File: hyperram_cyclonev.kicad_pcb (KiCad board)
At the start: 4 copper layers, 70.1 x 89.7 mm, 65 parts, among them IC1 AP63205WU, IC2 TXB0108PWR, IC3 S26KL128SDABHI020, IC4 W25Q32JVSSIQ_TR, IC5 S27KL0641DABHI020, J1 ASP-122952-01, J2 HDMI_A, J3 Conn_02x10_Odd_Even, J4 Conn_02x06_Odd_Even, J5 Conn_02x06_Top_Bottom, J6 Conn_02x06_Top_Bottom, J7 Conn_02x06_Top_Bottom, Q1 BSS138, Q2 BSS138

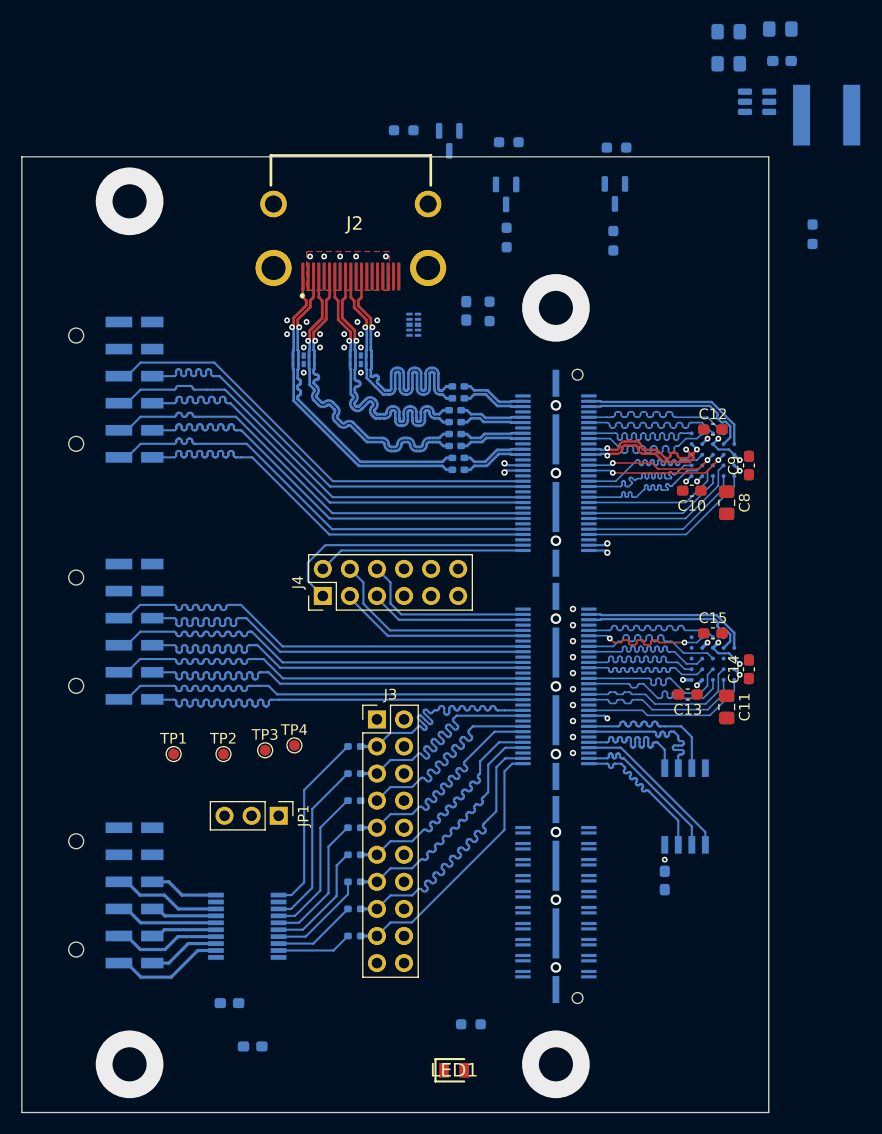
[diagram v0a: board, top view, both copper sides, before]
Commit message: Routed remaining HDMI signals. Routed DC/DC SWPS for +12V to +5V conversion
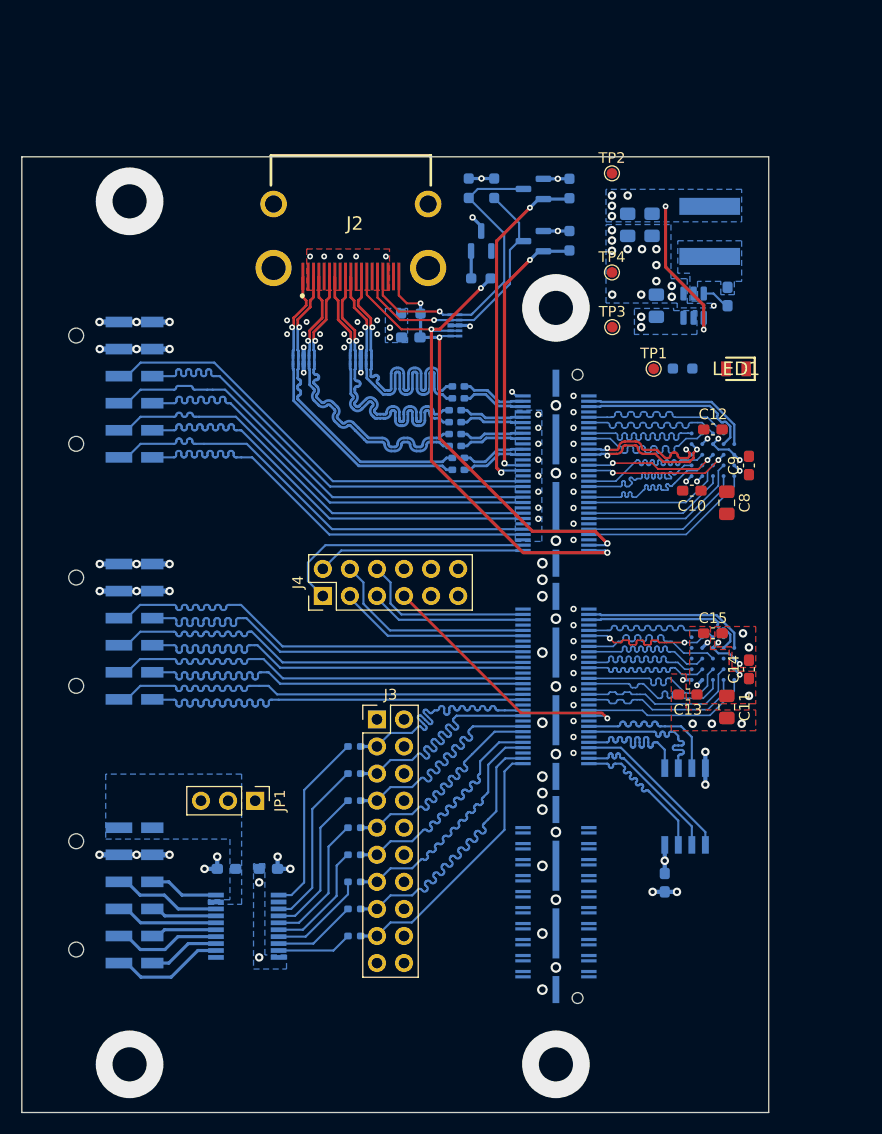
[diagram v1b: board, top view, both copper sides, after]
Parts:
- removed R7: 0R, Resistor_SMD:R_0603_1608Metric_Pad0.98x0.95mm_HandSolder
- moved LED1 70.9 mm to (239.4, 83.4), turned to 180 degrees
- moved TP2 65.6 mm to (227.8, 65.0)
- moved R10 64.6 mm to (234.4, 83.4), turned to 0 degrees
- moved TP1 57.7 mm to (231.7, 83.4)
- moved TP4 53.4 mm to (227.8, 74.3)
- moved TP3 51.3 mm to (227.8, 79.5)
- moved C2 26.6 mm to (231.9, 77.5), turned to 90 degrees
- moved C3 22.7 mm to (238.6, 76.6), turned to 90 degrees
- moved C5 22.0 mm to (231.5, 69.9), turned to -90 degrees
- moved IC1 20.0 mm to (235.4, 77.5), turned to 90 degrees
- moved C4 17.8 mm to (229.2, 69.9), turned to -90 degrees
- moved C7 16.8 mm to (191.6, 130.3)
- moved R5 15.7 mm to (215.5, 74.9)
- moved L1 15.5 mm to (236.9, 70.5), turned to 90 degrees
- moved R4 14.4 mm to (214.3, 66.4), turned to 90 degrees
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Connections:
- net Net-(IC1-SW) renamed /IC1_SW
- D2 pad 1: /hpdet -> /ddc_dat
- D2 pad 10: /hpdet -> /ddc_dat
- D2 pad 2: /ddc_dat -> /ddc_clk
- D2 pad 4: /ddc_clk -> /cec
- D2 pad 5: /cec -> /hpdet
- D2 pad 6: /cec -> /hpdet
- D2 pad 7: /ddc_clk -> /cec
- D2 pad 9: /ddc_dat -> /ddc_clk
- J1 pad 101: /hpdet -> /cec
- J1 pad 103: /cec -> /hpdet
- J2 pad 18: +5P -> +5V
- J4 pad 8: /cec -> GND
- R3 pad 2: +5P -> +5V
- R4 pad 2: +5P -> +5V
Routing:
- net /cec: track 1.80 -> 53.6 mm, vias 1 -> 3
- net /hpdet: track 1.82 -> 42.4 mm, vias 1 -> 3
- net GND: track 9.25 -> 46.8 mm, vias 36 -> 86
- net /ddc_dat_lv: track 1.81 -> 32.5 mm, vias 1 -> 2
- net /ddc_dat: track 0.00 -> 29.9 mm, vias 0 -> 1
- net /ddc_clk: track 0.00 -> 26.5 mm, vias 0 -> 1
- net /ddc_clk_lv: track 1.81 -> 26.0 mm, vias 1 -> 2
- net /debug_io6: track 1.84 -> 25.7 mm
- net +3V3: track 4.31 -> 26.6 mm, vias 17 -> 39
- net +5V: track 0.00 -> 16.5 mm, vias 0 -> 7
- net Net-(IC1-BST): track 0.00 -> 2.71 mm
- net Net-(D3-Pad2): track 0.00 -> 2.58 mm
- net /pmod3_io21: track 23.4 -> 24.9 mm
- net +12V: vias 0 -> 10
- added copper zone on B.Cu, net +12V
- added copper zone on B.Cu, net +3V3
- added copper zone on F.Cu, net +3V3
- added copper zone on B.Cu, net +5V
- added copper zone on B.Cu, net /IC1_SW
- added copper zone on B.Cu, net GND
- added copper zone on B.Cu, net VCCQ

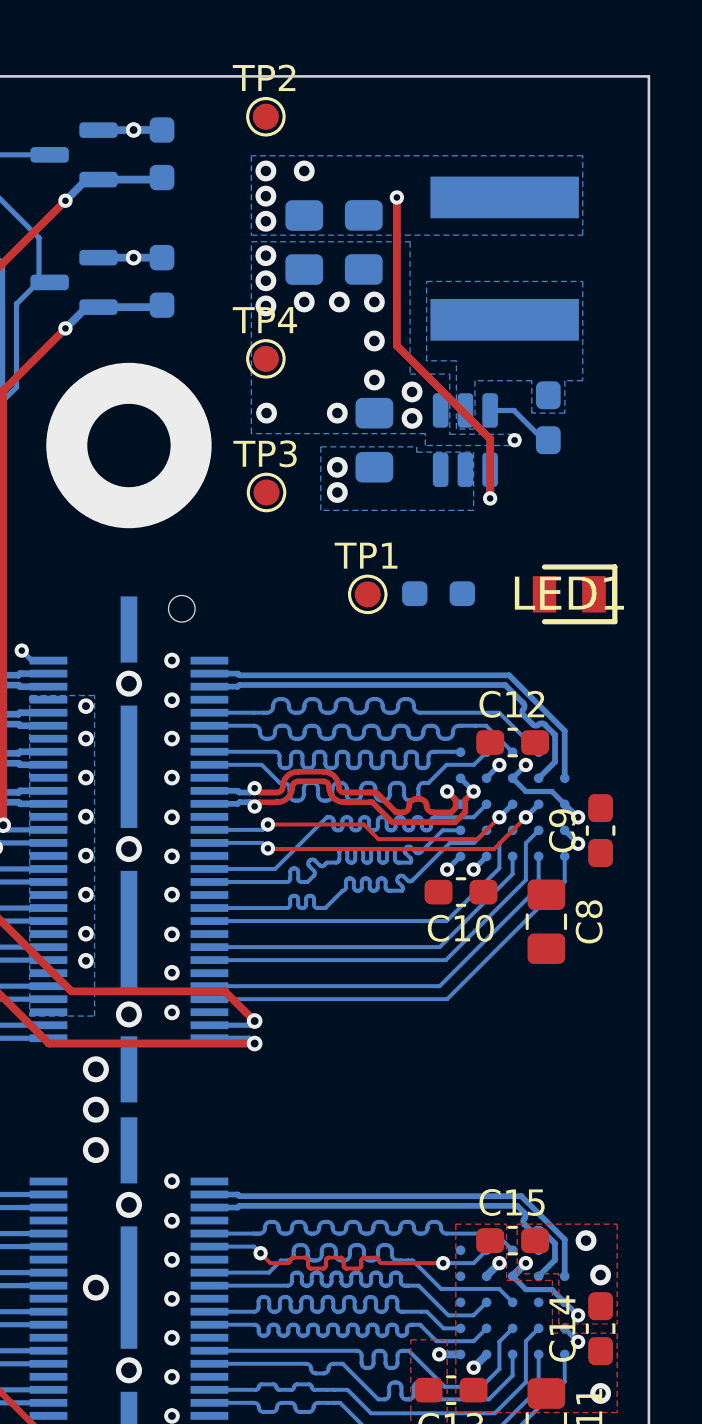
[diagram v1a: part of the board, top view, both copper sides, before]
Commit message: Added filled areas for GND and 3V3 supplying HyperRAM memory
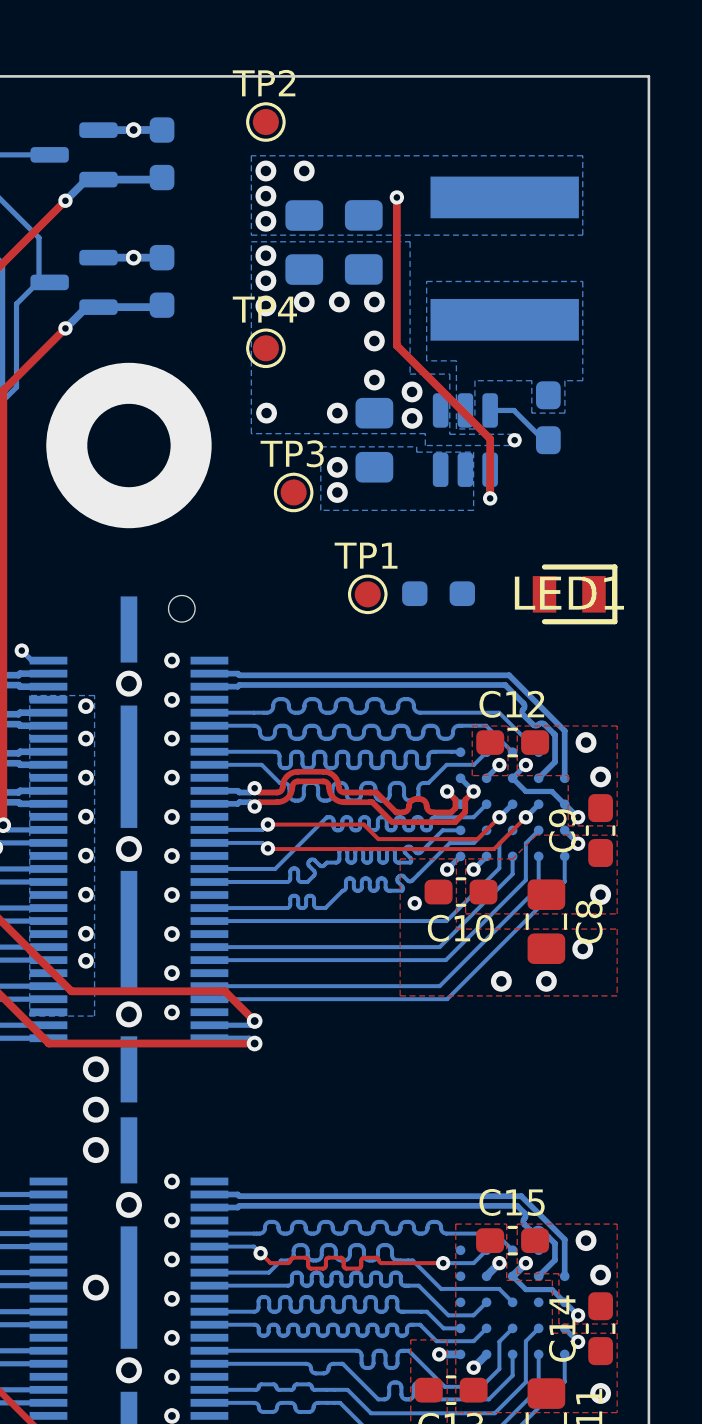
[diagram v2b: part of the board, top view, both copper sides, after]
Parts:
- moved TP3 1.04 mm to (228.8, 79.5)
- moved TP4 0.41 mm to (227.8, 73.9)
- moved TP2 0.20 mm to (227.8, 65.3)
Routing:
- net GND: vias 86 -> 92
- net +3V3: vias 39 -> 40

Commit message: Placed all local filled areas for 3V3, 5V, GND
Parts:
- moved LED1 65.2 mm to (236.1, 148.5)
- moved R10 61.4 mm to (235.2, 144.8), turned to -90 degrees
- moved TP1 5.86 mm to (236.2, 87.0)
- moved TP3 1.82 mm to (228.6, 81.3)
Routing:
- net +3V3: track 26.6 -> 50.6 mm, vias 40 -> 42
- net Net-(LED1-Pad2): track 0.00 -> 2.77 mm, vias 0 -> 1
- net GND: track 46.8 -> 49.3 mm, vias 92 -> 109
- net +12V: vias 10 -> 11
- added copper zone on F.Cu, net +12V
- added copper zone on F.Cu, net +5V

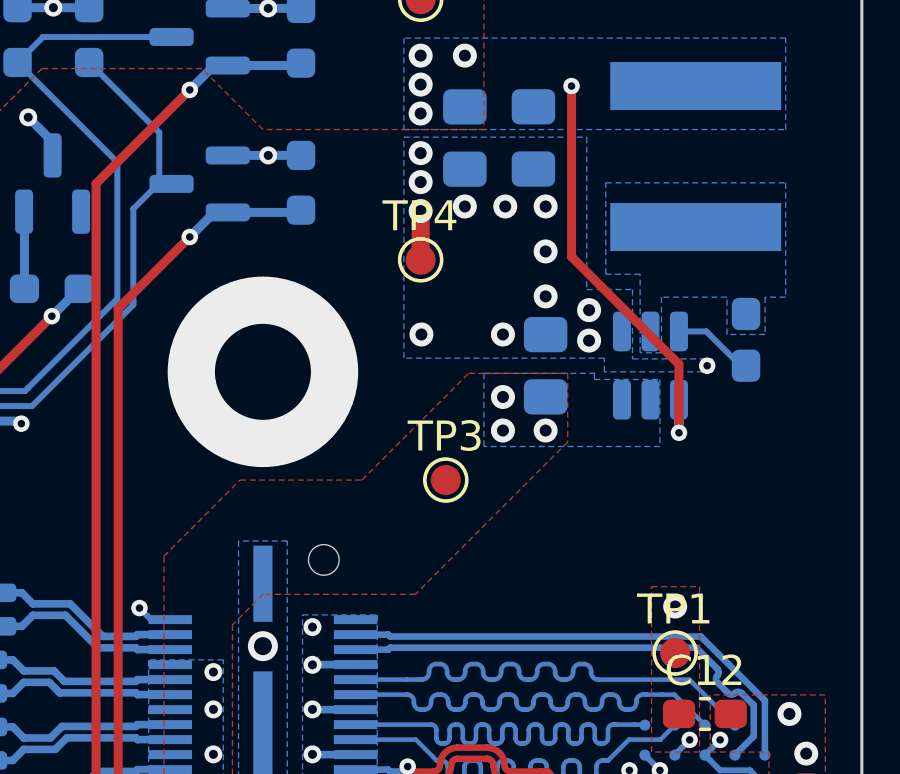
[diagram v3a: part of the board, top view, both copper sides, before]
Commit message: Added second filtering input capacitor for DC/DC converter
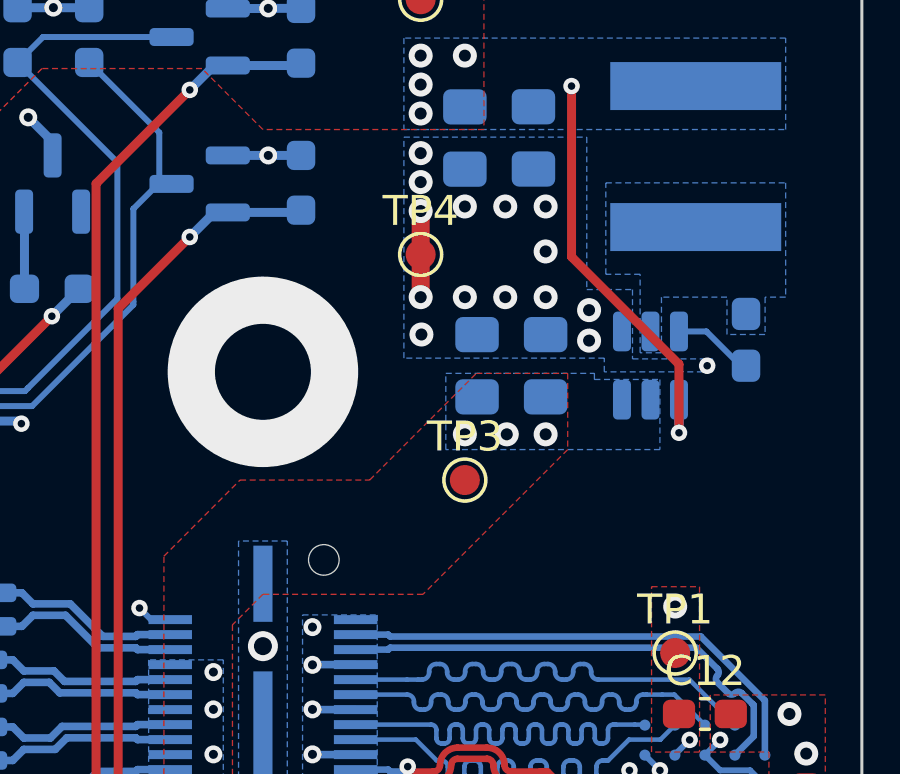
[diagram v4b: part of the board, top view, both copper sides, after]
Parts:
- added C25: 22uF, Capacitor_SMD:C_0805_2012Metric_Pad1.18x1.45mm_HandSolder, B.Cu at (229.6, 77.5)
- moved TP3 0.64 mm to (229.2, 81.3)
- moved TP4 0.18 mm to (227.8, 73.8)
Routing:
- net GND: track 49.3 -> 50.5 mm, vias 109 -> 111

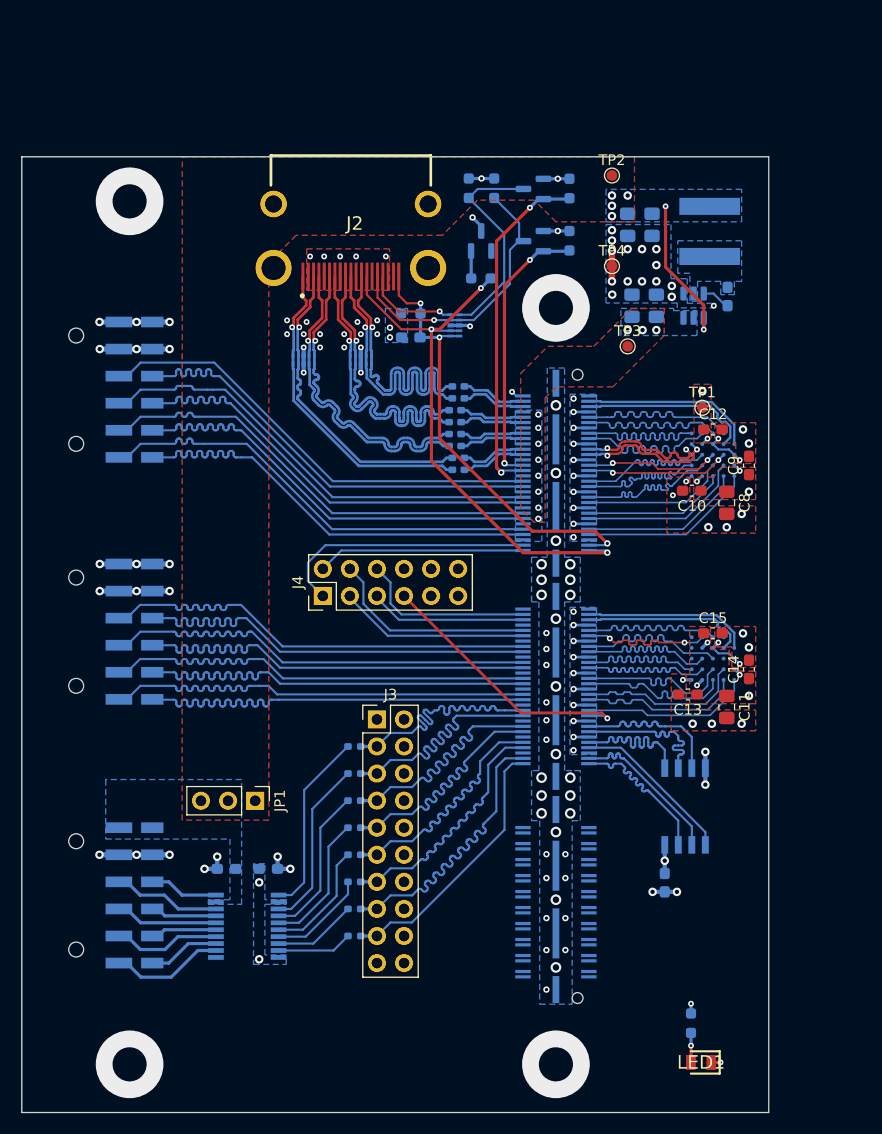
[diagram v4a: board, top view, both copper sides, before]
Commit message: Added GND and 3V3 fill areas
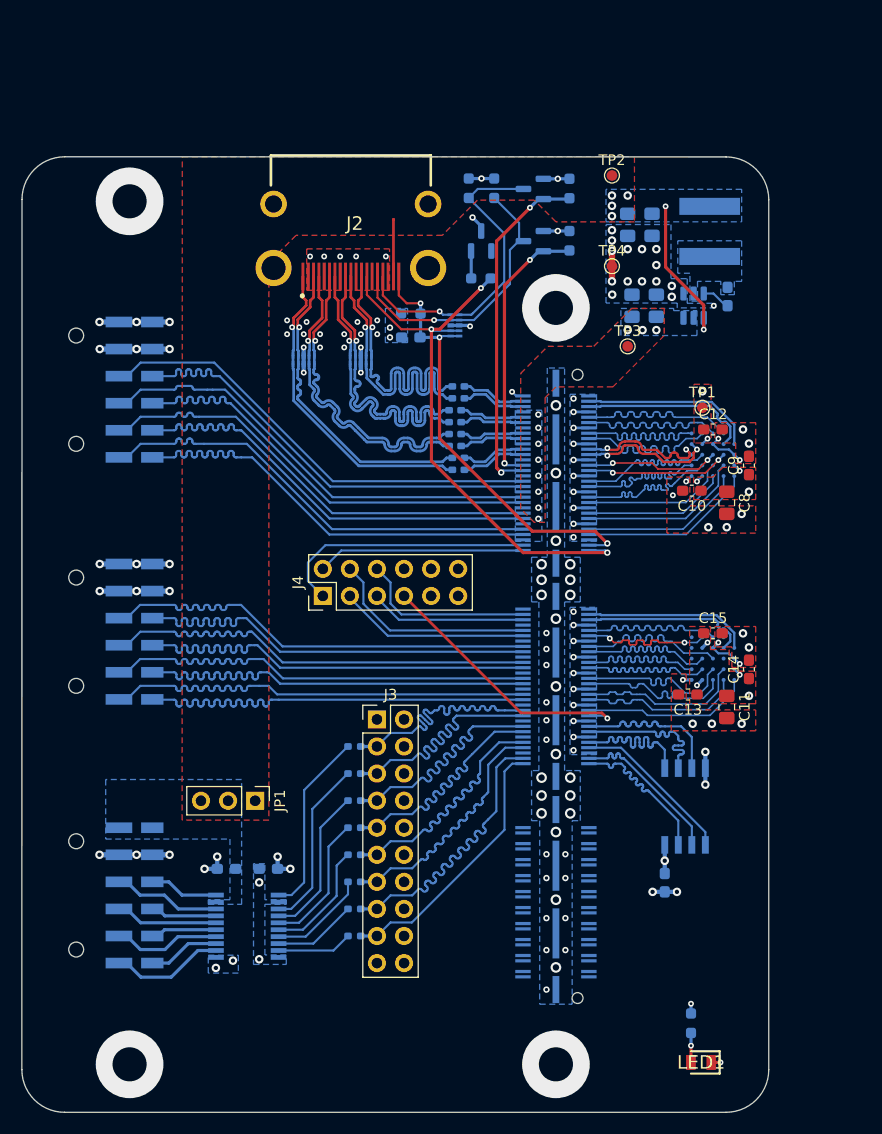
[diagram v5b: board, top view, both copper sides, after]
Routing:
- net +5V: track 16.5 -> 21.9 mm
- net GND: vias 111 -> 113
- added copper zone on In1.Cu, net +3V3
- added copper zone on In2.Cu, net GND
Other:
- board size 70.1 x 89.7 mm -> 70.1 x 89.6 mm

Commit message: Marked unused 12V pins as NC
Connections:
- J1 pad 100: +12V -> unconnected-(J1D-12V-Pad100)
- J1 pad 46: +12V -> unconnected-(J1D-12V-Pad46)
- J1 pad 52: +12V -> unconnected-(J1D-12V-Pad52)
- J1 pad 58: +12V -> unconnected-(J1D-12V-Pad58)
- J1 pad 64: +12V -> unconnected-(J1D-12V-Pad64)
- J1 pad 70: +12V -> unconnected-(J1D-12V-Pad70)
- J1 pad 76: +12V -> unconnected-(J1D-12V-Pad76)
- J1 pad 82: +12V -> unconnected-(J1D-12V-Pad82)
- J1 pad 88: +12V -> unconnected-(J1D-12V-Pad88)
- J1 pad 94: +12V -> unconnected-(J1D-12V-Pad94)
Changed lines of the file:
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@@
 	(net 121 "/pmod3_io18")
 	(net 122 "/IC1_SW")
+	(net 123 "unconnected-(J1D-12V-Pad64)")
+	(net 124 "unconnected-(J1D-12V-Pad52)")
+	(net 125 "unconnected-(J1D-12V-Pad76)")
+	(net 126 "unconnected-(J1D-12V-Pad100)")
+	(net 127 "unconnected-(J1D-12V-Pad58)")
+	(net 128 "unconnected-(J1D-12V-Pad88)")
+	(net 129 "unconnected-(J1D-12V-Pad46)")
+	(net 130 "unconnected-(J1D-12V-Pad70)")
+	(net 131 "unconnected-(J1D-12V-Pad82)")
+	(net 132 "unconnected-(J1D-12V-Pad94)")
 	(footprint "Connector_PinHeader_2.54mm:PinHeader_2x10_P2.54mm_Vertical"
 		(layer "F.Cu")
@@
 			(size 0.3 1.45)
 			(layers "B.Cu" "B.Paste" "B.Mask")
-			(net 3 "+12V")
+			(net 129 "unconnected-(J1D-12V-Pad46)")
 			(pinfunction "12V")
-			(pintype "passive")
+			(pintype "passive+no_connect")
 		)
 		(pad "47" smd rect
@@
 			(size 0.3 1.45)
 			(layers "B.Cu" "B.Paste" "B.Mask")
-			(net 3 "+12V")
+			(net 124 "unconnected-(J1D-12V-Pad52)")
 			(pinfunction "12V")
-			(pintype "passive")
+			(pintype "passive+no_connect")
 		)
 		(pad "53" smd rect
@@
 			(size 0.3 1.45)
 			(layers "B.Cu" "B.Paste" "B.Mask")
-			(net 3 "+12V")
+			(net 127 "unconnected-(J1D-12V-Pad58)")
 			(pinfunction "12V")
-			(pintype "passive")
+			(pintype "passive+no_connect")
 		)
 		(pad "59" smd rect
@@
 			(size 0.3 1.45)
 			(layers "B.Cu" "B.Paste" "B.Mask")
-			(net 3 "+12V")
+			(net 123 "unconnected-(J1D-12V-Pad64)")
 			(pinfunction "12V")
-			(pintype "passive")
+			(pintype "passive+no_connect")
 		)
 		(pad "65" smd rect
@@
 			(size 0.3 1.45)
 			(layers "B.Cu" "B.Paste" "B.Mask")
-			(net 3 "+12V")
+			(net 130 "unconnected-(J1D-12V-Pad70)")
 			(pinfunction "12V")
-			(pintype "passive")
+			(pintype "passive+no_connect")
 		)
 		(pad "71" smd rect
@@
 			(size 0.3 1.45)
 			(layers "B.Cu" "B.Paste" "B.Mask")
-			(net 3 "+12V")
+			(net 125 "unconnected-(J1D-12V-Pad76)")
 			(pinfunction "12V")
-			(pintype "passive")
+			(pintype "passive+no_connect")
 		)
 		(pad "77" smd rect
@@
 			(size 0.3 1.45)
 			(layers "B.Cu" "B.Paste" "B.Mask")
-			(net 3 "+12V")
+			(net 131 "unconnected-(J1D-12V-Pad82)")
 			(pinfunction "12V")
-			(pintype "passive")
+			(pintype "passive+no_connect")
 		)
 		(pad "83" smd rect
@@
 			(size 0.3 1.45)
 			(layers "B.Cu" "B.Paste" "B.Mask")
-			(net 3 "+12V")
+			(net 128 "unconnected-(J1D-12V-Pad88)")
 			(pinfunction "12V")
-			(pintype "passive")
+			(pintype "passive+no_connect")
 		)
 		(pad "89" smd rect
@@
 			(size 0.3 1.45)
 			(layers "B.Cu" "B.Paste" "B.Mask")
-			(net 3 "+12V")
+			(net 132 "unconnected-(J1D-12V-Pad94)")
 			(pinfunction "12V")
-			(pintype "passive")
+			(pintype "passive+no_connect")
 		)
 		(pad "95" smd rect
@@
 			(size 0.3 1.45)
 			(layers "B.Cu" "B.Paste" "B.Mask")
-			(net 3 "+12V")
+			(net 126 "unconnected-(J1D-12V-Pad100)")
 			(pinfunction "12V")
-			(pintype "passive")
+			(pintype "passive+no_connect")
 		)
 		(pad "101" smd rect
